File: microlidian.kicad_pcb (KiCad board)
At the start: 2 copper layers, 148.7 x 128.5 mm, 31 parts, among them J1 Conn_02x05_Odd_Even, J11 Backboard Conn 1, J12 Frontboard Conn 1, J13 Backboard Conn 2, J14 Frontboard Conn 2, J2 ST7789 TFT socket, J3 Expansion header, J4 ADS1015 digital side, J5 ADS1015 analog side, J7 TRS MIDI Out, SW1 RotaryEncoder_Switch, SW2 Back button, U1 SeeeduinoXIAO, U2 L78L05_TO92

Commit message: some minor updates
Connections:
- C1 pad 1: CV GND -> GND
- C2 pad 2: CV GND -> GND
- C3 pad 1: CV GND -> GND
- C4 pad 2: CV GND -> GND
- C5 pad 1: CV GND -> GND
- C6 pad 2: CV GND -> GND
- C7 pad 2: CV GND -> GND
- C8 pad 1: CV GND -> GND
- CV_Input_A1 pad S: CV GND -> GND
- CV_Input_A1 pad TN: CV GND -> GND
- CV_Input_B1 pad S: CV GND -> GND
- CV_Input_B1 pad TN: CV GND -> GND
- CV_Input_C1 pad S: CV GND -> GND
- CV_Input_C1 pad TN: CV GND -> GND
- J1 pad 3: CV GND -> GND
- J1 pad 4: CV GND -> GND
- J1 pad 5: CV GND -> GND
- J1 pad 6: CV GND -> GND
- J1 pad 7: CV GND -> GND
- J1 pad 8: CV GND -> GND
- J11 pad 12: CV GND -> GND
- J12 pad 12: CV GND -> GND
- J13 pad 3: CV GND -> GND
- J13 pad 7: CV GND -> GND
- J14 pad 3: CV GND -> GND
- J14 pad 7: CV GND -> GND
- J2 pad 1: CV GND -> GND
- J3 pad 15: CV GND -> GND
- J3 pad 16: CV GND -> GND
- J4 pad 5: CV GND -> GND
- J7 pad S: CV GND -> GND
- R1 pad 2: CV GND -> GND
- R2 pad 2: CV GND -> GND
- SW1 pad C: CV GND -> GND
- U1 pad 13: CV GND -> GND
- U2 pad 2: CV GND -> GND
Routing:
- net GND: track 0.00 -> 42.1 mm
- net CV GND: track 59.9 -> 17.8 mm
- added copper zone on B.Cu, net GND
- added copper zone on F.Cu, net GND
- removed copper zone on F.Cu, net CV GND

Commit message: updated from schematic, needs to be laid out again
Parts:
- J1: value Conn_02x05_Odd_Even -> Eurorack power
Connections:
- C1 pad 1: GND -> CV GND
- C2 pad 2: GND -> CV GND
- C3 pad 1: GND -> Backboard GND
- C4 pad 2: GND -> Backboard GND
- C5 pad 1: GND -> Backboard GND
- C5 pad 2: +5V -> Backboard +5V
- C6 pad 2: GND -> Backboard GND
- C7 pad 1: TFT lit Backboard -> Frontboard +3.3V
- C7 pad 2: GND -> CV GND
- C8 pad 2: +5V -> Backboard +5V
- CV_Input_A1 pad S: GND -> CV GND
- CV_Input_A1 pad TN: GND -> CV GND
- CV_Input_B1 pad S: GND -> CV GND
- CV_Input_B1 pad TN: GND -> CV GND
- CV_Input_C1 pad S: GND -> CV GND
- CV_Input_C1 pad TN: GND -> CV GND
- J1 pad 3: GND -> Backboard GND
- J1 pad 4: GND -> Backboard GND
- J1 pad 5: GND -> Backboard GND
- J1 pad 6: GND -> Backboard GND
- J1 pad 7: GND -> Backboard GND
- J1 pad 8: GND -> Backboard GND
- J11 pad 11: TFT lit Backboard -> Backboard +3.3V
- J11 pad 12: GND -> Backboard GND
- J12 pad 12: GND -> CV GND
- J13 pad 1: TFT lit Backboard -> Backboard +3.3V
- J13 pad 2: +5V -> Backboard +5V
- J13 pad 3: GND -> Backboard GND
- J13 pad 7: GND -> Backboard GND
- J14 pad 1: TFT lit Backboard -> Frontboard +3.3V
- J14 pad 2: +5V -> Frontboard +5V
- J14 pad 3: GND -> CV GND
- J14 pad 7: GND -> CV GND
- J2 pad 1: GND -> CV GND
- J2 pad 2: TFT lit Backboard -> Frontboard +3.3V
- J3 pad 11: +5V -> Backboard +5V
- J3 pad 13: TFT lit Backboard -> Backboard +3.3V
- J3 pad 15: GND -> Backboard GND
- J3 pad 16: GND -> Backboard GND
- J4 pad 1: +5V -> Backboard +5V
- J4 pad 5: GND -> Backboard GND
- J5 pad 1: +5V -> Backboard +5V
- J7 pad S: GND -> CV GND
- MIDI_OUT_Ra1 pad 2: TFT lit Backboard -> +3.3V
- R1 pad 2: GND -> CV GND
- R2 pad 2: GND -> CV GND
- SW1 pad C: GND -> CV GND
- SW1 pad S1: TFT lit Backboard -> Frontboard +3.3V
- U1 pad 12: TFT lit Backboard -> Backboard +3.3V
- U1 pad 13: GND -> Backboard GND
- U1 pad 14: +5V -> Backboard +5V
- U2 pad 1: +5V -> Backboard +5V
- U2 pad 2: GND -> Backboard GND
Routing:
- net TFT lit Backboard: track 311.7 -> 0.00 mm
- net (no net): track 0.00 -> 177.7 mm
- net Backboard +3.3V: track 0.00 -> 134.0 mm
- net Backboard +5V: track 0.00 -> 96.5 mm
- net +5V: track 96.5 -> 0.00 mm
- net GND: track 42.1 -> 0.00 mm
- net Backboard GND: track 0.00 -> 42.1 mm

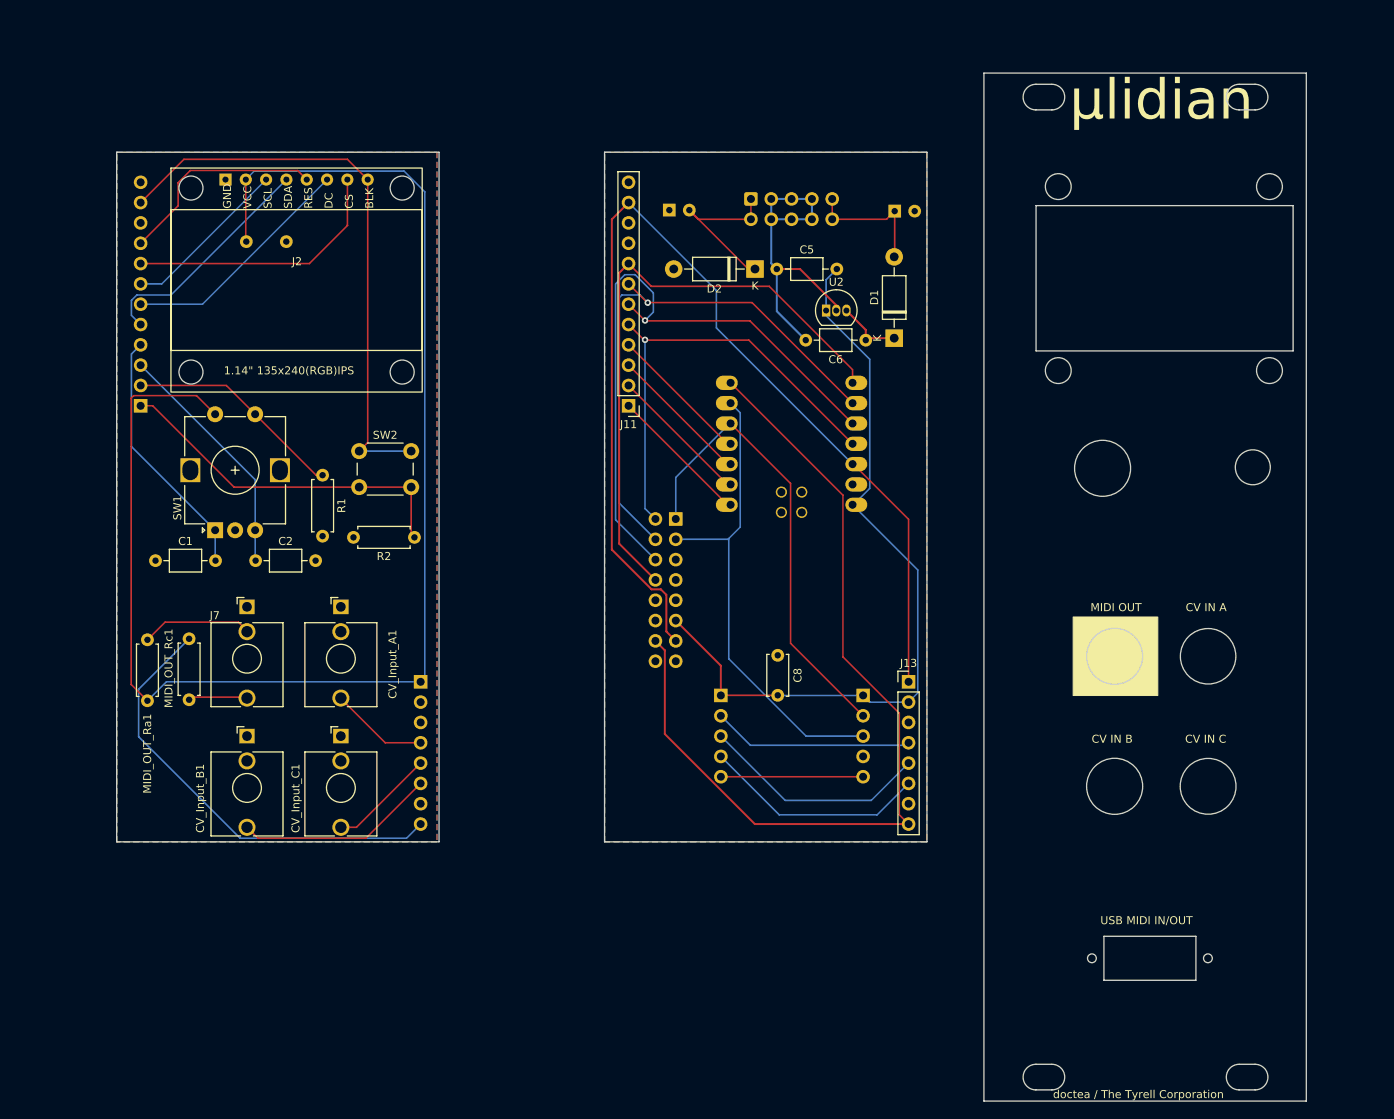
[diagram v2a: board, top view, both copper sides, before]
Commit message: completely relaid out the pcb
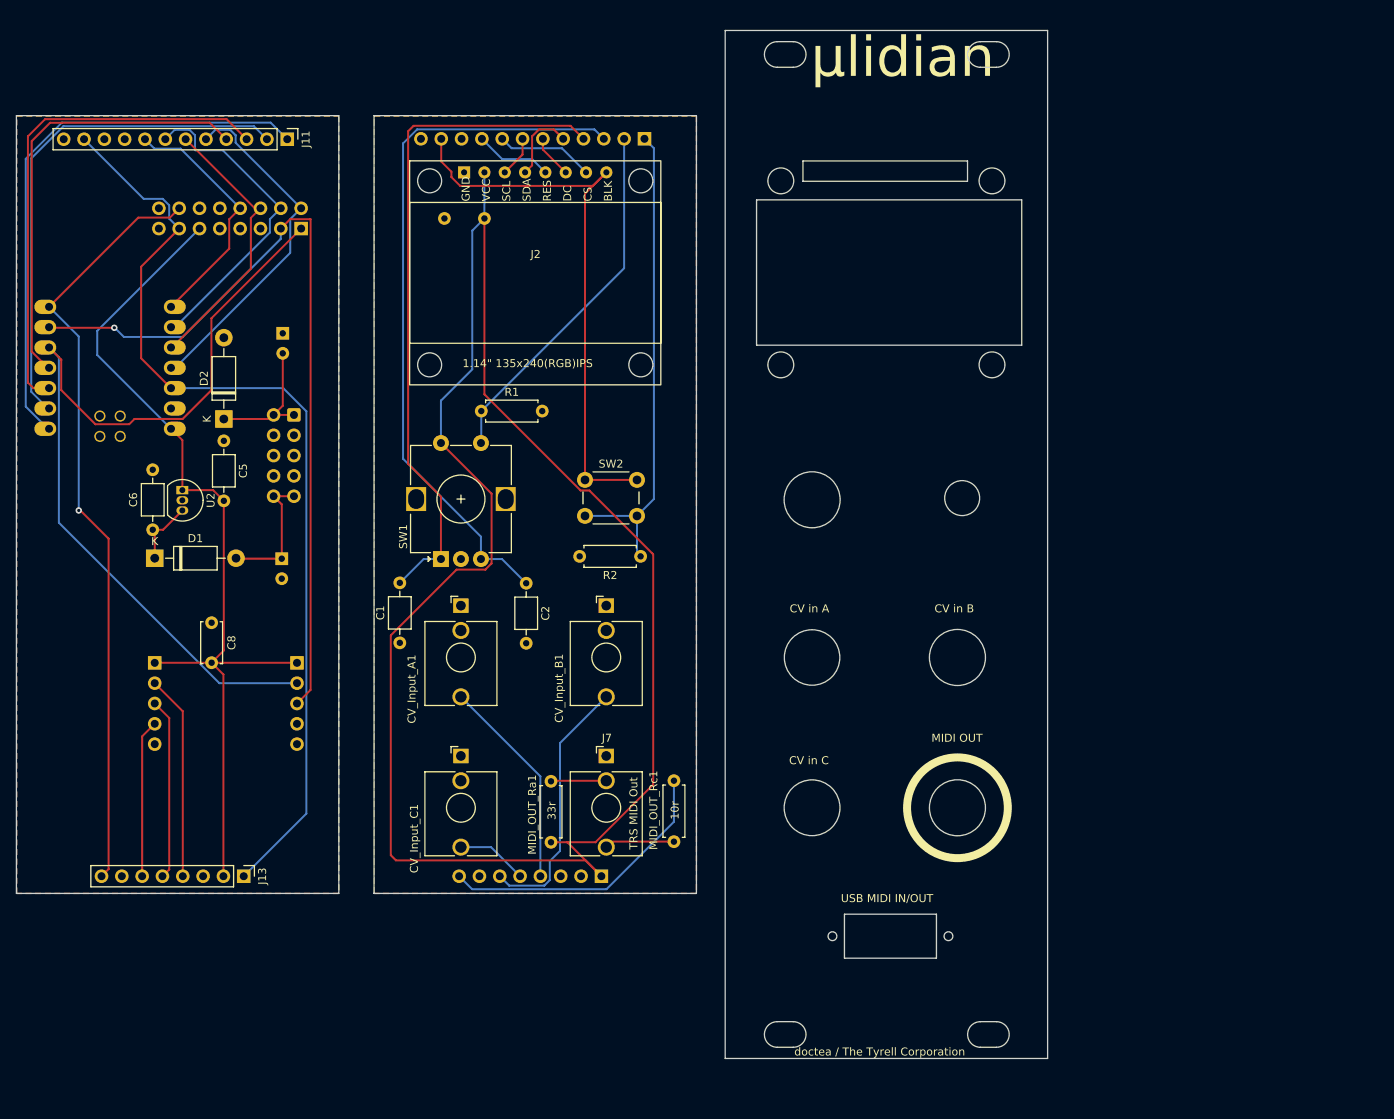
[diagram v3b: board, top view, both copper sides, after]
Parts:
- moved D1 96.4 mm to (55.5, 101.5), turned to 0 degrees
- moved C6 92.2 mm to (55.3, 98.0), turned to 90 degrees
- moved C4 88.1 mm to (71.4, 101.6), turned to -90 degrees
- moved J13 86.6 mm to (66.6, 141.3), turned to -90 degrees
- moved U1 85.7 mm to (49.9, 77.7)
- moved U2 83.5 mm to (59.0, 93.0), turned to -90 degrees
- moved C5 72.4 mm to (64.2, 86.9), turned to -90 degrees
- moved J12 71.3 mm to (116.7, 49.1), turned to 90 degrees
- moved C8 70.9 mm to (62.6, 109.6)
- moved J5 70.9 mm to (55.5, 114.6)
- moved J4 70.9 mm to (73.3, 114.6)
- moved D2 69.0 mm to (64.2, 84.2), turned to 90 degrees
- moved J1 63.2 mm to (72.9, 83.6), turned to 180 degrees
- moved MIDI_OUT_Rc1 63.1 mm to (120.4, 137.0)
- moved J3 59.2 mm to (73.8, 60.3), turned to 90 degrees
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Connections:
- C1 pad 1: CV GND -> Backboard GND
- C2 pad 2: CV GND -> Backboard GND
- C7 pad 2: CV GND -> Backboard GND
- CV_Input_A1 pad S: CV GND -> Backboard GND
- CV_Input_A1 pad TN: CV GND -> Backboard GND
- CV_Input_B1 pad S: CV GND -> Backboard GND
- CV_Input_B1 pad TN: CV GND -> Backboard GND
- CV_Input_C1 pad S: CV GND -> Backboard GND
- CV_Input_C1 pad TN: CV GND -> Backboard GND
- J12 pad 12: CV GND -> Backboard GND
- J14 pad 3: CV GND -> Backboard GND
- J14 pad 7: CV GND -> Backboard GND
- J2 pad 1: CV GND -> Backboard GND
- J5 pad 5: CV GND -> Backboard GND
- J7 pad S: CV GND -> Backboard GND
- MIDI_OUT_Ra1 pad 2: +3.3V -> Frontboard +3.3V
- R1 pad 2: CV GND -> Backboard GND
- R2 pad 2: CV GND -> Backboard GND
- SW1 pad C: CV GND -> Backboard GND
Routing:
- net Frontboard +3.3V: track 0.00 -> 226.9 mm
- net (no net): track 177.7 -> 0.00 mm
- net Encoder left Frontboard: track 30.3 -> 89.2 mm
- net i2c SDA: track 58.1 -> 113.6 mm
- net Back button Backboard: track 17.5 -> 70.5 mm
- net Encoder right Frontboard: track 31.7 -> 84.4 mm
- net Encoder button Backboard: track 17.5 -> 64.1 mm
- net TFT DC Backboard: track 80.7 -> 35.1 mm, vias 1 -> 0
- net TFT CS Backboard: track 77.1 -> 31.4 mm
- net Encoder left Backboard: track 17.5 -> 63.0 mm
- net Backboard GND: track 42.1 -> 0.00 mm
- net i2c SCL: track 60.5 -> 101.4 mm, vias 0 -> 1
- net Encoder right Backboard: track 17.5 -> 55.4 mm
- net SPI CLK Backboard: track 70.4 -> 40.9 mm, vias 1 -> 0
- net TFT DC Frontboard: track 29.8 -> 5.38 mm
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- added copper zone on B.Cu, net Backboard GND
- added copper zone on F.Cu, net Backboard GND
- removed copper zone on B.Cu, net GND
- removed copper zone on F.Cu, net GND
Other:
- board size 148.7 x 128.5 mm -> 128.9 x 128.5 mm
- board text added: "CV in A"
- board text added: "CV in B"
- board text added: "CV in C"
- board text removed: "CV IN A"
- board text removed: "CV IN B"
- board text removed: "CV IN C"

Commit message: minor tweaks
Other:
- board text added: "USB end"
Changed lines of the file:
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@@
     (effects (font (size 1.5 1.5) (thickness 0.3) bold) (justify left bottom mirror))
+  )
+  (gr_text "USB end" (at 52.7812 90.5256) (layer "B.SilkS")
+    (effects (font (size 1 1) (thickness 0.15)) (justify left bottom mirror))
   )
   (gr_text "3v" (at 58.311 63.6718 -90) (layer "B.SilkS")
@@
   (segment (start 104.0388 49.125) (end 104.0388 50.46329) (width 0.25) (layer "F.Cu") (net 15))
   (segment (start 104.0388 50.46329) (end 106.89539 53.31988) (width 0.25) (layer "F.Cu") (net 15))
-  (segment (start 92.6084 53.2384) (end 92.6084 53.90689) (width 0.25) (layer "F.Cu") (net 17))
   (segment (start 115.80559 91.76188) (end 109.30559 91.76188) (width 0.25) (layer "F.Cu") (net 17))
-  (segment (start 92.6084 53.90689) (end 93.71791 55.0164) (width 0.25) (layer "F.Cu") (net 17))
-  (segment (start 110.27887 55.0164) (end 111.97539 53.31988) (width 0.25) (layer "F.Cu") (net 17))
-  (segment (start 91.3388 51.9688) (end 92.6084 53.2384) (width 0.25) (layer "F.Cu") (net 17))
-  (segment (start 93.71791 55.0164) (end 110.27887 55.0164) (width 0.25) (layer "F.Cu") (net 17))
+  (segment (start 91.3388 52.63729) (end 91.3388 49.125) (width 0.25) (layer "F.Cu") (net 17))
+  (segment (start 93.71791 55.0164) (end 91.3388 52.63729) (width 0.25) (layer "F.Cu") (net 17))
+  (segment (start 110.27887 55.0164) (end 93.71791 55.0164) (width 0.25) (layer "F.Cu") (net 17))
   (segment (start 109.30559 55.98968) (end 111.97539 53.31988) (width 0.25) (layer "F.Cu") (net 17))
-  (segment (start 91.3388 49.125) (end 91.3388 51.9688) (width 0.25) (layer "F.Cu") (net 17))
+  (segment (start 111.97539 53.31988) (end 110.27887 55.0164) (width 0.25) (layer "F.Cu") (net 17))
   (segment (start 109.30559 91.76188) (end 109.30559 55.98968) (width 0.25) (layer "F.Cu") (net 17))
   (segment (start 112.64707 136.9822) (end 111.96339 137.66588) (width 0.25) (layer "F.Cu") (net 18))
@@
     )
   )
-  (group "" (id a2415efe-1946-4346-b781-3f071b889dc2)
+  (group "" (id 9ba59d72-def7-4c48-a47f-115897acab69)
     (members
       84b72671-b5e9-4841-8972-14fc9985875f
+      8a591b77-03e9-4d19-8061-d2dc83057681
       cbf6af6f-eb81-4583-99a4-97dfb73d00eb
     )

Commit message: move labels a lil
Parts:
- U2: value L78L05_TO92 -> L78L05
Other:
- outline, holes or cut-outs redrawn
- board text added: "back"
- board text added: "doctea / Tyrell Corporation"
- board text removed: "doctea / The Tyrell Corporation"
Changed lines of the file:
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@@
         (effects (font (size 1 1) (thickness 0.15)))
     )
-    (fp_text value "L78L05_TO92" (at -2.667 2.921 90) (layer "F.Fab")
+    (fp_text value "L78L05" (at 5.0292 -0.8172 180) (layer "F.SilkS")
         (effects (font (size 1 1) (thickness 0.15)))
     )
@@
         (effects (font (size 1 1) (thickness 0.15)))
     )
-    (fp_text value "10K" (at 3.7084 0.0508) (layer "F.Fab")
-        (effects (font (size 1 1) (thickness 0.15)))
-    )
-    (fp_text user "${REFERENCE}" (at 3.8624 0.06) (layer "F.Fab")
+    (fp_text value "10K" (at 3.7084 0.0508) (layer "F.SilkS")
         (effects (font (size 1 1) (thickness 0.15)))
     )
@@
     (property "ki_keywords" "diode Schottky")
     (attr through_hole)
-    (fp_text reference "D1" (at 5.08 -2.47) (layer "F.SilkS")
+    (fp_text reference "D1" (at 5.2832 2.6924) (layer "F.SilkS")
         (effects (font (size 1 1) (thickness 0.15)))
     )
-    (fp_text value "1N5817" (at 5.334 -3.81) (layer "F.Fab")
-        (effects (font (size 1 1) (thickness 0.15)))
+    (fp_text value "1N5817" (at 5.588 0.1016) (layer "F.SilkS")
+        (effects (font (size 0.8 0.8) (thickness 0.15)))
     )
     (fp_text user "K" (at 0 -2.1) (layer "F.SilkS")
@@
         (effects (font (size 1 1) (thickness 0.15)))
     )
-    (fp_text user "${REFERENCE}" (at 5.47 0) (layer "F.Fab")
-        (effects (font (size 1 1) (thickness 0.15)))
-    )
     (fp_line (start 1.34 0) (end 2.36 0)
       (stroke (width 0.12) (type solid)) (layer "F.SilkS"))
@@
     (property "ki_keywords" "capacitor cap")
     (attr through_hole)
-    (fp_text reference "C5" (at 3.75 -2.42 90) (layer "F.SilkS")
+    (fp_text reference "C5" (at 3.496 2.2606 90) (layer "F.SilkS")
         (effects (font (size 1 1) (thickness 0.15)))
     )
-    (fp_text value "1uF" (at 3.75 2.42 90) (layer "F.Fab")
+    (fp_text value "1uF" (at 3.5722 -0.0254 90) (layer "F.SilkS")
         (effects (font (size 1 1) (thickness 0.15)))
     )
-    (fp_text user "${REFERENCE}" (at 3.75 0 90) (layer "F.Fab")
-        (effects (font (size 0.76 0.76) (thickness 0.114)))
-    )
     (fp_line (start 1.04 0) (end 1.73 0)
       (stroke (width 0.12) (type solid)) (layer "F.SilkS"))
@@
         (effects (font (size 1 1) (thickness 0.15)))
     )
-    (fp_text value "100n" (at 2.5 2.5 90) (layer "F.Fab")
-        (effects (font (size 1 1) (thickness 0.15)))
-    )
-    (fp_text user "${REFERENCE}" (at 2.46 0.1524 90) (layer "F.Fab")
-        (effects (font (size 1 1) (thickness 0.15)))
+    (fp_text value "100n" (at 2.5272 -0.077474 90) (layer "F.SilkS")
+        (effects (font (size 0.9 0.9) (thickness 0.15)))
     )
     (fp_line (start -0.12 -1.37) (end -0.12 -1.055)
@@
         (effects (font (size 1 1) (thickness 0.15)))
     )
-    (fp_text value "10K" (at 3.81 2.37) (layer "F.Fab")
-        (effects (font (size 1 1) (thickness 0.15)))
-    )
-    (fp_text user "${REFERENCE}" (at 3.81 0) (layer "F.Fab")
+    (fp_text value "10K" (at 3.683 0.0508) (layer "F.SilkS")
         (effects (font (size 1 1) (thickness 0.15)))
     )
@@
         (effects (font (size 1 1) (thickness 0.15)))
     )
-    (fp_text value "10uF" (at 3.75 2.42 90) (layer "F.Fab")
+    (fp_text value "10uF" (at 3.7338 0.127 90) (layer "F.SilkS")
         (effects (font (size 1 1) (thickness 0.15)))
     )
@@
         (effects (font (size 1 1) (thickness 0.15)))
     )
-    (fp_text value "1N5817" (at 5.08 2.47 90) (layer "F.Fab")
-        (effects (font (size 1 1) (thickness 0.15)))
+    (fp_text value "1N5817" (at 5.5626 0.1016 90) (layer "F.SilkS")
+        (effects (font (size 0.8 0.8) (thickness 0.15)))
     )
     (fp_text user "K" (at 0 -2.1 90) (layer "F.SilkS")
         (effects (font (size 1 1) (thickness 0.15)))
     )
-    (fp_text user "${REFERENCE}" (at 5.47 0 90) (layer "F.Fab")
-        (effects (font (size 1 1) (thickness 0.15)))
-    )
     (fp_text user "K" (at 0 -2.1 90) (layer "F.Fab")
         (effects (font (size 1 1) (thickness 0.15)))
@@
   (gr_line (start 160.732 159.484) (end 158.732 159.484)
     (stroke (width 0.05) (type solid)) (layer "Edge.Cuts"))
-  (gr_rect (start 141.73739 146.0498) (end 153.23739 151.5498)
+  (gr_rect (start 141.23239 146.0498) (end 152.73239 151.5498)
     (stroke (width 0.05) (type default)) (fill none) (layer "Edge.Cuts"))
   (gr_circle (center 155.86089 113.959331) (end 158.40089 116.372331)
@@
   (gr_arc (start 158.732 40.184) (mid 157.132 38.584) (end 158.732 36.984)
     (stroke (width 0.05) (type solid)) (layer "Edge.Cuts"))
-  (gr_circle (center 140.23739 148.7998) (end 140.78739 148.7998)
+  (gr_circle (center 139.73239 148.7998) (end 140.28239 148.7998)
     (stroke (width 0.05) (type default)) (fill none) (layer "Edge.Cuts"))
   (gr_rect (start 82.934968 46.23089) (end 123.234968 143.45189)
@@
   (gr_circle (center 133.782706 54.380272) (end 134.959106 55.487072)
     (stroke (width 0.05) (type default)) (fill none) (layer "Edge.Cuts"))
-  (gr_circle (center 154.73739 148.7998) (end 155.28739 148.7998)
+  (gr_circle (center 154.23239 148.7998) (end 154.78239 148.7998)
     (stroke (width 0.05) (type default)) (fill none) (layer "Edge.Cuts"))
   (gr_rect (start 130.75049 56.758272) (end 163.89749 74.919272)
@@
     (effects (font (size 1 1) (thickness 0.15)) (justify left bottom mirror))
   )
-  (gr_text "CV in A" (at 134.884343 108.440844) (layer "F.SilkS")
+  (gr_text "CV in A" (at 131.2672 117.8814 90) (layer "F.SilkS")
+    (effects (font (size 1.5 1.5) (thickness 0.15)) (justify left bottom))
+  )
+  (gr_text "back" (at 159.8422 94.488) (layer "F.SilkS")
     (effects (font (size 1 1) (thickness 0.15)) (justify left bottom))
   )
-  (gr_text "USB MIDI IN/OUT" (at 141.28739 144.6598) (layer "F.SilkS")
+  (gr_text "USB MIDI IN/OUT" (at 140.78239 144.6598) (layer "F.SilkS")
     (effects (font (size 1 1) (thickness 0.15)) (justify left bottom))
   )
@@
     )
   )
-  (gr_text "MIDI OUT" (at 152.6022 124.6176) (layer "F.SilkS")
+  (gr_text "MIDI OUT" (at 163.8808 129.7178 -90) (layer "F.SilkS")
     (effects (font (size 1 1) (thickness 0.15)) (justify left bottom))
   )
-  (gr_text "CV in B" (at 152.982914 108.440844) (layer "F.SilkS")
-    (effects (font (size 1 1) (thickness 0.15)) (justify left bottom))
+  (gr_text "CV in B" (at 162.1536 109.855 -90) (layer "F.SilkS")
+    (effects (font (size 1.5 1.5) (thickness 0.15)) (justify left bottom))
   )
-  (gr_text "CV in C" (at 134.812914 127.42159) (layer "F.SilkS")
-    (effects (font (size 1 1) (thickness 0.15)) (justify left bottom))
+  (gr_text "CV in C" (at 131.318 136.8552 90) (layer "F.SilkS")
+    (effects (font (size 1.5 1.5) (thickness 0.15)) (justify left bottom))
   )
-  (gr_text "doctea / The Tyrell Corporation" (at 135.462 163.834) (layer "F.SilkS")
+  (gr_text "doctea / Tyrell Corporation" (at 136.8044 163.5506) (layer "F.SilkS")
     (effects (font (size 1 1) (thickness 0.15)) (justify left bottom))
   )
@@
   (group "" (id dc8fa51f-eb1e-4b13-b27b-2bf3b7b59ab2)
     (members
+      2cc2e96c-69ec-454e-bef5-9d5ea330cea2
       69de8739-739d-4f9c-847c-e8564e14259b
       725e94ed-625d-4a8a-bf21-1a64bc1a077b
